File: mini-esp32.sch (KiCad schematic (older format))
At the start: 50 parts, among them J1 BAT, J2 USB_B_Micro, J5 Conn_01x18, J6 Conn_01x18, Q1 AO3401A, Q2 S8050, Q3 S8050, Q4 2N7002, Q5 AO3400A, Q6 AO3400A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

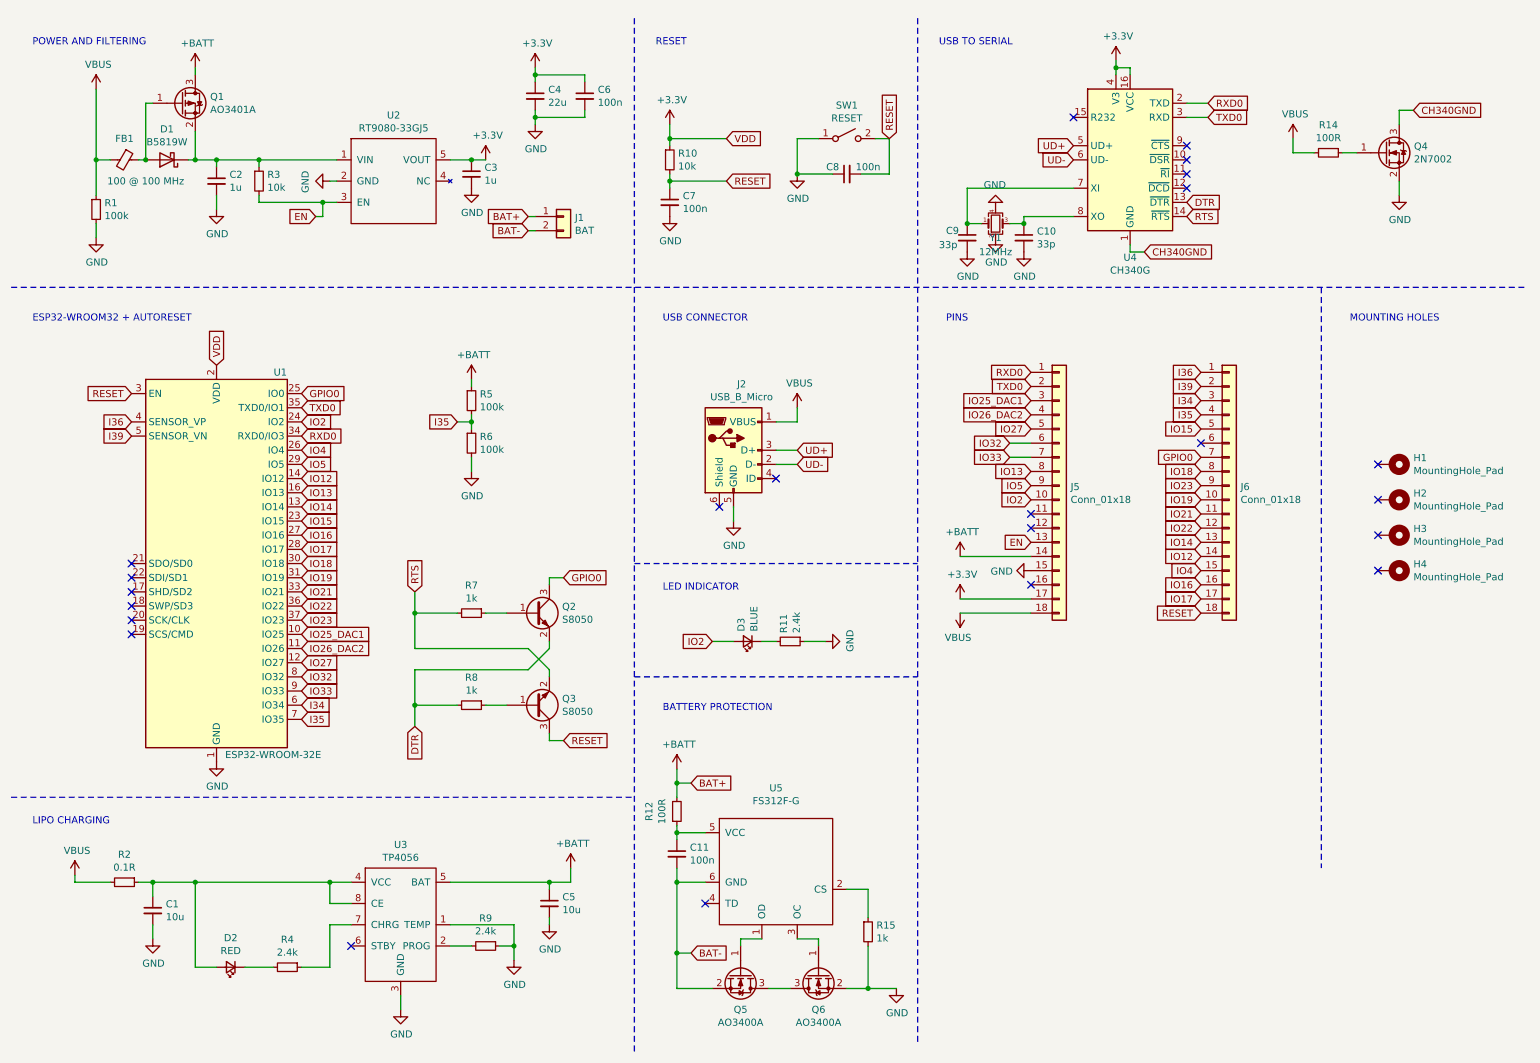
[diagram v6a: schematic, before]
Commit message: Fix CH340G. Backside pin numbering.
 - Crystal cap to 22pF from 33pf like the reference implementation.
 - Fix CH340G VCC to use an extra LDO instead of using RT9080 with a N MOSFET. N MOSFET to the GND seems to interfere with the CH340G's USB signalling.
 - Backside silkscreen pin numbering
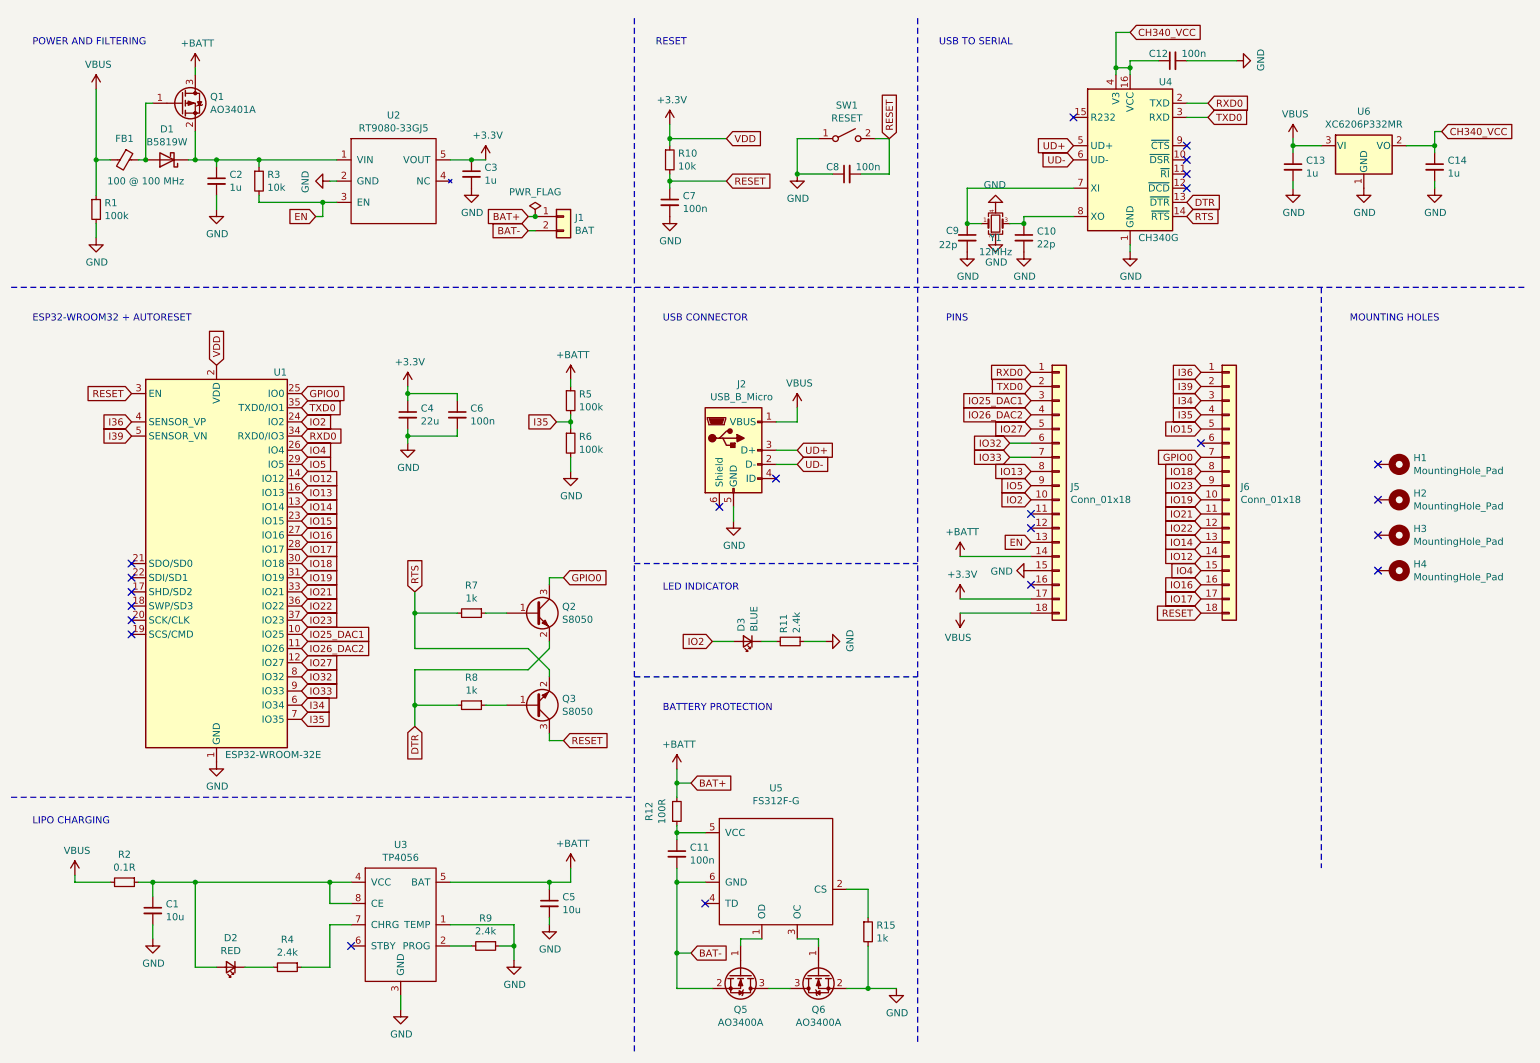
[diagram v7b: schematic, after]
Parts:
- removed Q4: 2N7002, Package_TO_SOT_SMD:SOT-23, symbol Transistor_FET:2N7002
- removed R14: 100R, Resistor_SMD:R_0402_1005Metric, symbol Device:R_Small
- added C12: 100n, Capacitor_SMD:C_0402_1005Metric, symbol Device:C_Small
- added C13, C14: 1u, Capacitor_SMD:C_0402_1005Metric, symbol Device:C_Small
- added U6: XC6206P332MR, Package_TO_SOT_SMD:SOT-23, symbol Regulator_Linear:XC6206PxxxMR
- C10, C9: value 33p -> 22p; LCSC Part # C1562 -> C1555
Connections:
- net CH340GND is gone; now on net GND: U4.1 (GND)
- net +3V3: no longer U4.16 (VCC), U4.4 (V3)
- net GND: now also C12.2, C13.2, C14.2, U6.1 (GND)
- net VBUS: now also C13.1, U6.3 (VI)
- new net CH340_VCC: C12.1, C14.1, U4.16 (VCC), U4.4 (V3), U6.2 (VO)
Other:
- moved on the sheet: C4, C6, R5, R6

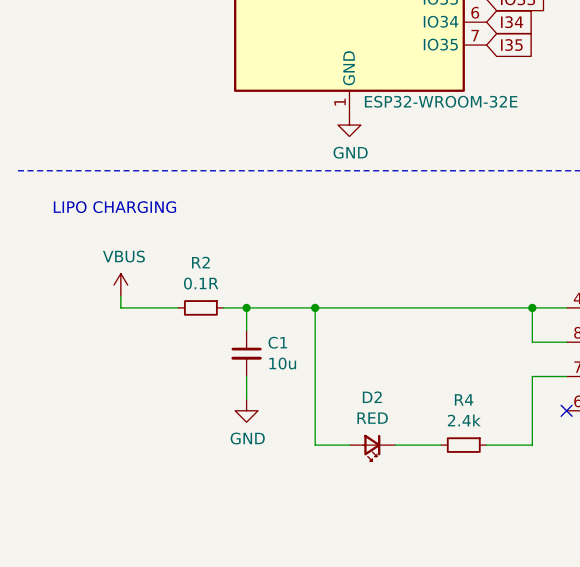
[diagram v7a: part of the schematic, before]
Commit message: Change 0.1R TP4056 resistor to a diode
Helps with the heat issues of TP4056.
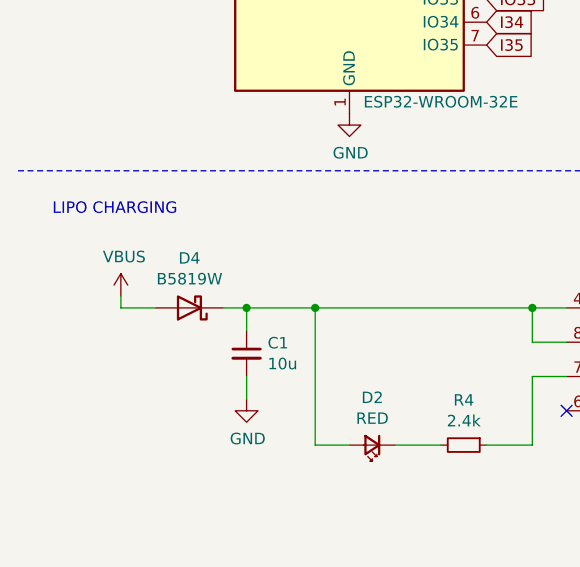
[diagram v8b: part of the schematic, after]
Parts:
- removed R2: 0.1R, Resistor_SMD:R_1206_3216Metric, symbol Device:R_Small
- added D4: B5819W, Diode_SMD:D_SOD-123, symbol Device:D_Schottky
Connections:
- net VBUS: now also D4.2 (A)
- net at C1.1, D2.2 (A), U3.4 (VCC)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: now also D4.1 (K)
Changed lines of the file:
@@
 	1    0    0    -1
-$EndComp
-$Comp
-L Device:R_Small R2
-U 1 1 5F9C4288
-P 1300 6600
-F 0 "R2" V 1104 6600 50  0000 C CNN
-F 1 "0.1R" V 1195 6600 50  0000 C CNN
-F 2 "Resistor_SMD:R_1206_3216Metric" H 1300 6600 50  0001 C CNN
-F 3 "~" H 1300 6600 50  0001 C CNN
-F 4 "C25334" H 1300 6600 50  0001 C CNN "LCSC Part #"
-	1    1300 6600
-	0    1    1    0
 $EndComp
 Wire Wire Line
 	950  6550 950  6600
-Wire Wire Line
-	950  6600 1200 6600
 $Comp
 L Device:C_Small C1
@@
 $EndComp
 Connection ~ 4200 1900
+$Comp
+L Device:D_Schottky D4
+U 1 1 5FCD5A57
+P 1250 6600
+F 0 "D4" H 1250 6383 50  0000 C CNN
+F 1 "B5819W" H 1250 6474 50  0000 C CNN
+F 2 "Diode_SMD:D_SOD-123" H 1250 6600 50  0001 C CNN
+F 3 "~" H 1250 6600 50  0001 C CNN
+F 4 "C8598" H 1250 6600 50  0001 C CNN "LCSC Part #"
+	1    1250 6600
+	-1   0    0    1
+$EndComp
+Wire Wire Line
+	950  6600 1100 6600
 $EndSCHEMATC
